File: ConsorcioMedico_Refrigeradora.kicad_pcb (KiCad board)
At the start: 2 copper layers, 260 x 70 mm, 111 parts, among them J1 BatteryHolder, J10 Screw_Terminal_01x01, J11 Screw_Terminal_01x01, J12 Screw_Terminal_01x01, J13 Screw_Terminal_01x01, J2 USART, J3 Screw_Terminal_01x01, J4 SWD, J5 Screw_Terminal_01x01, J6 Screw_Terminal_01x02, J7 Screw_Terminal_01x02, J8 Screw_Terminal_01x01, J9 Screw_Terminal_01x01, K1 HF46F-G/012-HS1T, K2 T9AS1D12-12, K4 HF46F-G/012-HS1T, Q1 MMBT3904, Q2 MMBT3904, Q3 MMBT3904, Q4 MMBT3904, Q5 BSS123, Q6 BSS123, Q7 BSS123, U1 STM32F411RETx, U2 IRM-02, U3 LDL1117, U4 INA350, U5 INA350, Y1 8Mhz, Y2 32.768khz/12.5pF

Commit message: SCH: Falta definir los capacitores de entrada, colocar el footprint del diodo e inductor. PCB: Falta acomodar algunos componentes.
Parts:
- removed D2, D3: RED, 1-Led:LED_0805
- removed J12, J13, J5: Screw_Terminal_01x01, 1-Pad:PAD_D2.60mm_Drill1.4mm
- added C27: 1uF 50V, 1-Capacitor:C_0805_2012Metric, B.Cu at (77.3, 94.9)
- added C28: 1uF 50V, 1-Capacitor:C_0805_2012Metric, B.Cu at (93.1, 96.4)
- added C29: 470uF, 1-Capacitor:C_1206_3216Metric, B.Cu at (47.5, 121.4)
- added C31: 1uF, 1-Capacitor:C_0805_2012Metric, B.Cu at (42.4, 127.7)
- added C32: 1uF, 1-Capacitor:C_0805_2012Metric, B.Cu at (42.4, 130.7)
- added C33: 180uF, 1-Capacitor:C_1206_3216Metric, B.Cu at (47.5, 128.1)
- added D10: 1N4148WS, Diode_SMD:D_SOD-323, B.Cu at (180.8, 85.9)
- added D11: RED, 1-Led:LED_0805, B.Cu at (71.8, 83.6)
- added D12: RED, 1-Led:LED_0805, B.Cu at (88.6, 83.7)
- added J16: Screw_Terminal_01x02, 1-Terminal-Block:DG504-5.08-02P_or_SMKDS 2,5-2-5.08, B.Cu at (72.6, 72.6)
- added J17: Screw_Terminal_01x02, 1-Terminal-Block:DG504-5.08-02P_or_SMKDS 2,5-2-5.08, B.Cu at (89.4, 72.5)
- added J19: Screw_Terminal_01x02, 1-Terminal-Block:DG504-5.08-02P_or_SMKDS 2,5-2-5.08, B.Cu at (165.0, 72.7)
- added JP1: Bridge1, Jumper:SolderJumper-2_P1.3mm_Open_Pad1.0x1.5mm, B.Cu at (85.3, 76.4)
- added JP2: Bridge1, Jumper:SolderJumper-2_P1.3mm_Open_Pad1.0x1.5mm, B.Cu at (68.5, 76.5)
- added K3: HF46F-G/012-HS1T, 1-Relay:Relay_HONGFA_SPST-NO_20.5x7x15.3mm, B.Cu at (155.1, 84.3)
- added Q8: BSS806, Package_TO_SOT_SMD:SOT-23, B.Cu at (183.8, 89.8)
- added R40: 10K, 1-Resistor:R_0805_2012Metric, B.Cu at (158.2, 89.6)
- added R41: 10K, 1-Resistor:R_0805_2012Metric, B.Cu at (180.8, 89.7)
- added R42: 6.2k, 1-Resistor:R_1206_3216Metric, B.Cu at (72.2, 79.3)
- added R43: 2.4k, 1-Resistor:R_0805_2012Metric, B.Cu at (71.6, 81.5)
- added R44: 1k, 1-Resistor:R_0805_2012Metric, B.Cu at (77.3, 92.8)
- added R45: 22k, 1-Resistor:R_0805_2012Metric, B.Cu at (77.3, 90.7)
- added R46: 6.2k, 1-Resistor:R_1206_3216Metric, B.Cu at (89.0, 79.4)
- added R47: 2.4k, 1-Resistor:R_0805_2012Metric, B.Cu at (88.4, 81.7)
- added R48: 1k, 1-Resistor:R_0805_2012Metric, B.Cu at (93.1, 94.4)
- added R49: 22k, 1-Resistor:R_0805_2012Metric, B.Cu at (93.1, 92.4)
- added R50: 2k, 1-Resistor:R_0805_2012Metric, B.Cu at (68.4, 72.8)
- added R51: 2k, 1-Resistor:R_0805_2012Metric, B.Cu at (85.3, 72.9)
- added U6: LTV-357T, Package_SO:SO-4_4.4x3.6mm_P2.54mm, B.Cu at (77.3, 85.1)
- added U7: LTV-357T, Package_SO:SO-4_4.4x3.6mm_P2.54mm, B.Cu at (93.0, 86.9)
- added U8: LM2594HVM-5.0, Package_SO:SOIC-8_3.9x4.9mm_P1.27mm, B.Cu at (40.4, 122.9)
- D1: value L-144IDT -> LED_0805; footprint 1-Led:LED_3.9x1.9mm -> 1-Led:LED_0805; moved to B.Cu
- D9: value LED_0805 -> L-144IDT; footprint 1-Led:LED_0805 -> 1-Led:LED_3.9x1.9mm
- J10, J11, J8, J9: value Screw_Terminal_01x01 -> Screw_Terminal_01x02; footprint 1-Pad:PAD_D2.60mm_Drill1.4mm -> 1-Terminal-Block:DG504-5.08-02P_or_SMKDS 2,5-2-5.08
- J3: value Screw_Terminal_01x01 -> USART; footprint 1-Pad:PAD_D2.60mm_Drill1.4mm -> 1-Pinhead:PinHeader_1x04_P2.54mm_Vertical
- Q5, Q6, Q7: value BSS123 -> BSS806
- R14: value 120R -> 1k
- R2, R4, R5: value 1k -> 330
- R24, R29: value 1k -> 2.2k
- R35, R36, R38: value 330 -> 1k
- R39: value 10K -> 220R
- R6: value 1k -> 120R
- moved R20 317.9 mm to (258.7, 101.7), turned to -90 degrees
- moved R19 293.3 mm to (233.9, 105.3), turned to 90 degrees
- moved D5 287.6 mm to (222.1, 90.0), turned to -90 degrees
- moved D4 267.4 mm to (201.8, 85.7)
- moved Q6 265.9 mm to (216.3, 89.5), turned to 0 degrees
- moved R15 264.7 mm to (209.5, 105.3), turned to 90 degrees
- moved Q5 254.6 mm to (204.7, 89.2), turned to 0 degrees
- moved R34 253.4 mm to (213.2, 89.5), turned to -90 degrees
- moved R32 246.5 mm to (211.1, 89.5), turned to -90 degrees
- moved R18 243.8 mm to (184.3, 105.2), turned to 90 degrees
- moved R33 242.0 mm to (201.6, 89.2), turned to -90 degrees
- moved R31 234.9 mm to (199.5, 89.2), turned to -90 degrees
- moved J4 230.2 mm to (145.2, 131.0), turned to -90 degrees
- moved D6 224.0 mm to (158.8, 85.9)
- moved R17 220.2 mm to (160.5, 105.5), turned to 90 degrees
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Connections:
- C13 pad 1: +5V -> +12V
- J2 pad 2: MCU_RX6 -> MCU_RX1
- J2 pad 3: MCU_TX6 -> MCU_TX1
- J3 pad 1: Net-(J3-Pin_1) -> +3.3V
- K1 pad 3: Net-(J9-Pin_1) -> Net-(J8-Pin_1)
- K1 pad 4: Net-(J8-Pin_1) -> Net-(J8-Pin_2)
- K2 pad 1: Net-(D6-A) -> Net-(D5-A)
- K2 pad 3: Net-(J13-Pin_1) -> Net-(J9-Pin_1)
- K2 pad 4: Net-(J12-Pin_1) -> Net-(J9-Pin_2)
- K4 pad 1: Net-(D5-A) -> Net-(D10-A)
- K4 pad 3: Net-(J11-Pin_1) -> Net-(J10-Pin_1)
- K4 pad 4: Net-(J10-Pin_1) -> Net-(J10-Pin_2)
- R1 pad 2: Net-(D9-A) -> Net-(D1-A)
- R11 pad 1: E -> C
- R11 pad 2: Net-(LED1-E) -> Net-(LED1-C)
- R12 pad 1: F -> B
- R12 pad 2: Net-(LED1-F) -> Net-(LED1-B)
- R13 pad 1: G -> A
- R13 pad 2: Net-(LED1-G) -> Net-(LED1-A)
- R14 pad 1: DP -> DIG1
- R14 pad 2: Net-(LED1-DP) -> Net-(Q1-B)
- R15 pad 1: Button_Touch -> Button_Buzzer
- R16 pad 1: Button_Up -> Button_Touch
- R17 pad 1: Button_Buzzer -> Button_Up
- R2 pad 1: DIG1 -> LED_Defrost
- R2 pad 2: Net-(Q1-B) -> Net-(D7-PadA)
- R21 pad 2: Net-(J7-Pin_1) -> Net-(J6-Pin_1)
- R22 pad 1: Net-(J7-Pin_1) -> Net-(J6-Pin_1)
- R23 pad 1: Net-(J7-Pin_2) -> Net-(J6-Pin_2)
- R24 pad 1: RTD1 -> I2C3_SCL
- R24 pad 2: Net-(D2-A) -> +3.3V
- R25 pad 1: Net-(J7-Pin_2) -> Net-(J6-Pin_2)
- R26 pad 2: Net-(J6-Pin_1) -> Net-(J7-Pin_1)
- R27 pad 1: Net-(J6-Pin_1) -> Net-(J7-Pin_1)
- R28 pad 1: Net-(J6-Pin_2) -> Net-(J7-Pin_2)
- R29 pad 1: RTD2 -> I2C3_SDA
- R29 pad 2: Net-(D3-A) -> +3.3V
- R30 pad 1: Net-(J6-Pin_2) -> Net-(J7-Pin_2)
- R31 pad 1: RELAY_Q1 -> Relay_Fan
- R32 pad 1: RELAY_Q3 -> Relay_Compressor
- R32 pad 2: Net-(Q7-G) -> Net-(Q6-G)
- R34 pad 2: Net-(Q7-G) -> Net-(Q6-G)
- R35 pad 1: LED_Defrost -> DIG2
- R35 pad 2: Net-(D1-PadA) -> Net-(Q2-B)
- R36 pad 1: LED_Door -> DIG3
- R36 pad 2: Net-(D7-PadA) -> Net-(Q3-B)
- R37 pad 1: RELAY_Q2 -> Relay_Light
- R37 pad 2: Net-(Q6-G) -> Net-(Q7-G)
- R38 pad 1: LED_TempAlarm -> DIG4
- R38 pad 2: Net-(D8-PadA) -> Net-(Q4-B)
- R39 pad 1: GND -> Relay_Calefac
- R39 pad 2: Net-(Q6-G) -> Net-(Q8-G)
- R4 pad 1: DIG2 -> LED_Door
- R4 pad 2: Net-(Q2-B) -> Net-(D8-PadA)
- R5 pad 1: DIG3 -> LED_TempAlarm
- R5 pad 2: Net-(Q3-B) -> Net-(D9-PadA)
- R6 pad 1: DIG4 -> DP
- R6 pad 2: Net-(Q4-B) -> Net-(LED1-DP)
- R7 pad 1: A -> G
- R7 pad 2: Net-(LED1-A) -> Net-(LED1-G)
- R8 pad 1: B -> F
- R8 pad 2: Net-(LED1-B) -> Net-(LED1-F)
- R9 pad 1: C -> E
- R9 pad 2: Net-(LED1-C) -> Net-(LED1-E)
- U1 pad 10: unconnected-(U1-PC2-Pad10) -> DIG2
- U1 pad 11: unconnected-(U1-PC3-Pad11) -> DIG1
- U1 pad 2: unconnected-(U1-PC13-Pad2) -> Relay_Calefac
- U1 pad 24: unconnected-(U1-PC4-Pad24) -> RTD1
- U1 pad 25: unconnected-(U1-PC5-Pad25) -> RTD2
- U1 pad 33: STATUS_LED -> LED_Status
- U1 pad 34: unconnected-(U1-PB13-Pad34) -> LED_Defrost
- U1 pad 35: unconnected-(U1-PB14-Pad35) -> LED_Door
- U1 pad 36: unconnected-(U1-PB15-Pad36) -> LED_TempAlarm
- U1 pad 38: unconnected-(U1-PC7-Pad38) -> DIG_IN_1
- U1 pad 39: unconnected-(U1-PC8-Pad39) -> DIG_IN_0
- U1 pad 40: unconnected-(U1-PC9-Pad40) -> I2C3_SDA
- U1 pad 41: DIG1 -> I2C3_SCL
- U1 pad 42: DIG2 -> MCU_TX1
- U1 pad 43: DIG3 -> MCU_RX1
- U1 pad 44: DIG4 -> USB_DM
- U1 pad 45: LED_Status -> USB_DP
- U1 pad 46: LED_Defrost -> SWDIO
- U1 pad 49: LED_Door -> SWCLK
- U1 pad 50: LED_TempAlarm -> unconnected-(U1-PA15-Pad50)
- U1 pad 51: unconnected-(U1-PC10-Pad51) -> Relay_Fan
- U1 pad 52: unconnected-(U1-PC11-Pad52) -> Relay_Light
- U1 pad 53: unconnected-(U1-PC12-Pad53) -> Relay_Compressor
- U1 pad 55: Button_Buzzer -> SWO
- U1 pad 56: Button_Touch -> Button_Buzzer
- U1 pad 57: Button_Up -> Button_Touch
- U1 pad 58: Button_Down -> Button_Up
- U1 pad 59: Button_Cooling -> Button_Down
- U1 pad 61: Button_Light -> Button_Cooling
- U1 pad 62: unconnected-(U1-PB9-Pad62) -> Button_Light
- U1 pad 8: unconnected-(U1-PC0-Pad8) -> DIG4
- U1 pad 9: unconnected-(U1-PC1-Pad9) -> DIG3
- U2 pad +V: +5V -> +12V
- U2 pad AC1: Net-(J3-Pin_1) -> Net-(J11-Pin_1)
- U2 pad AC2: Net-(J5-Pin_1) -> Net-(J11-Pin_2)

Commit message: SCH: Se cambió el IRM, se colocó filtro en la entrada AC, se modificó la fuente switching LM, se corrigieron algunos errores de diseño. PCB: Se terminó el placement de los componentes
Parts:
- removed C31, C32: 1uF, 1-Capacitor:C_0805_2012Metric
- removed C33: 180uF, 1-Capacitor:C_1206_3216Metric
- removed U2: IRM-02, 1-Supply_Module-Eagle:IRM-02
- added C30: 0.1uF 275VAC, Capacitor_THT:C_Rect_L18.0mm_W5.0mm_P15.00mm_FKS3_FKP3, B.Cu at (122.0, 65.9)
- added C35: 220uF 25V, Capacitor_SMD:CP_Elec_6.3x7.7, B.Cu at (101.0, 103.0)
- added D2: SS34B, 1-Diode:D_SMB, B.Cu at (101.0, 93.3)
- added F1: Fuse, Fuse:Fuseholder_TR5_Littelfuse_No560_No460, B.Cu at (138.1, 69.1)
- added L1: YSPI1050-680M, Inductor_SMD:L_10.4x10.4_H4.8, B.Cu at (110.2, 95.3)
- added L2: UU9.8-10mH, 1-Inductor:UU9.8-10mH, B.Cu at (119.1, 80.7)
- added R52: 1k, 1-Resistor:R_0603_1608Metric, B.Cu at (94.4, 88.0)
- added RV1: FNR6045S680, Varistor:RV_Disc_D12mm_W5.1mm_P7.5mm, B.Cu at (126.5, 66.7)
- added U9: HLK-PMx, 1-Module:HLK-PM12, B.Cu at (106.9, 84.2)
- C13: value 10uF -> 470uF 25V; footprint 1-Capacitor:C_1206_3216Metric -> Capacitor_SMD:CP_Elec_10x10
- C29: value 470uF -> 220uF 25V; footprint 1-Capacitor:C_1206_3216Metric -> Capacitor_SMD:CP_Elec_6.3x7.7
- K2: value T9AS1D12-12 -> AZ2150-1A-12DEF; footprint 1-Relay:Relay_TE-Connectivity_SPST-NO_32.5x27.4x27.9mm -> 1-Relay:Relay_Zettler_SPST-NO_31.8x26.9x19.1mm
- moved J11 120.9 mm to (143.4, 72.7)
- moved C12 102.9 mm to (29.8, 116.4), turned to 180 degrees
- moved J1 102.2 mm to (26.7, 116.3)
- moved J3 85.5 mm to (81.8, 131.5)
- moved C13 65.6 mm to (87.4, 92.6), turned to -90 degrees
- moved R2 62.9 mm to (15.9, 96.5), turned to 180 degrees
- moved U8 62.7 mm to (95.7, 93.4), turned to 90 degrees
- moved R4 59.8 mm to (15.9, 105.5), turned to 180 degrees
- moved R5 56.4 mm to (15.8, 114.4), turned to 180 degrees
- moved C28 54.2 mm to (39.5, 89.0), turned to -90 degrees
- moved R48 51.9 mm to (41.5, 89.0), turned to 90 degrees
- moved R47 51.6 mm to (36.8, 81.8)
- moved J17 51.6 mm to (37.8, 72.7)
- moved R46 51.6 mm to (37.4, 79.5)
- moved D12 51.6 mm to (37.0, 83.8)
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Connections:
- C29 pad 1: GND -> +12V
- C29 pad 2: +12V -> GND
- D10 pad 1: +5V -> +12V
- D4 pad 1: +5V -> +12V
- D5 pad 1: +5V -> +12V
- D6 pad 1: +5V -> +12V
- K1 pad 2: +5V -> +12V
- K2 pad 2: +5V -> +12V
- K3 pad 2: +5V -> +12V
- K4 pad 2: +5V -> +12V
- U8 pad 5: unconnected-(U8-~{ON}/OFF-Pad5) -> Net-(U8-~{ON}/OFF)

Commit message: Se guarda avance
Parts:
- moved J1 2.11 mm to (26.9, 118.4)
- moved C12 2.11 mm to (30.0, 118.5)
- moved C6 2.09 mm to (69.3, 125.1)
- moved C7 2.09 mm to (70.9, 125.1)
- moved U1 1.34 mm to (66.6, 116.8)
- moved C20 1.34 mm to (63.9, 125.2)
- moved C4 1.34 mm to (58.3, 111.0)
- moved C11 1.34 mm to (71.7, 107.8)
- moved C15 1.34 mm to (75.2, 123.7)
- moved C17 1.34 mm to (80.2, 113.2)
- moved C18 1.34 mm to (80.2, 110.2)
- moved D1 1.34 mm to (55.6, 123.7)
- moved R1 1.34 mm to (55.5, 121.7)
- moved C10 1.34 mm to (73.5, 107.8)
- moved C5 1.34 mm to (58.3, 112.6)
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
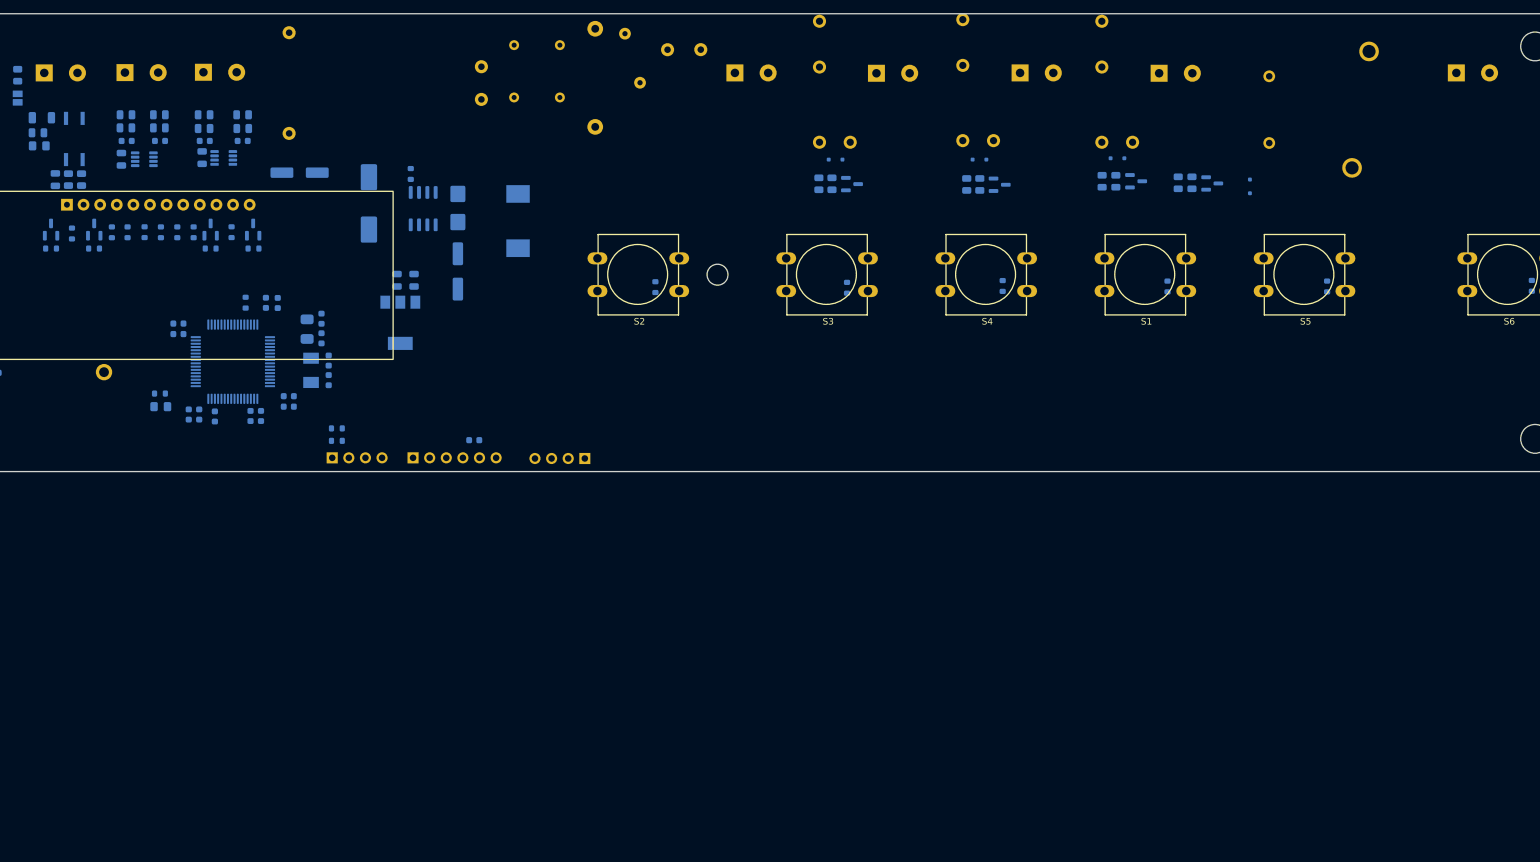
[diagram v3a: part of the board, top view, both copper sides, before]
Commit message: SCH: Se cambian la bornera por terminales, se añade un disparo más para el compressor (falta conectarlo al uC), falta modificar, se cambia la fuente switching por otra de menos costo
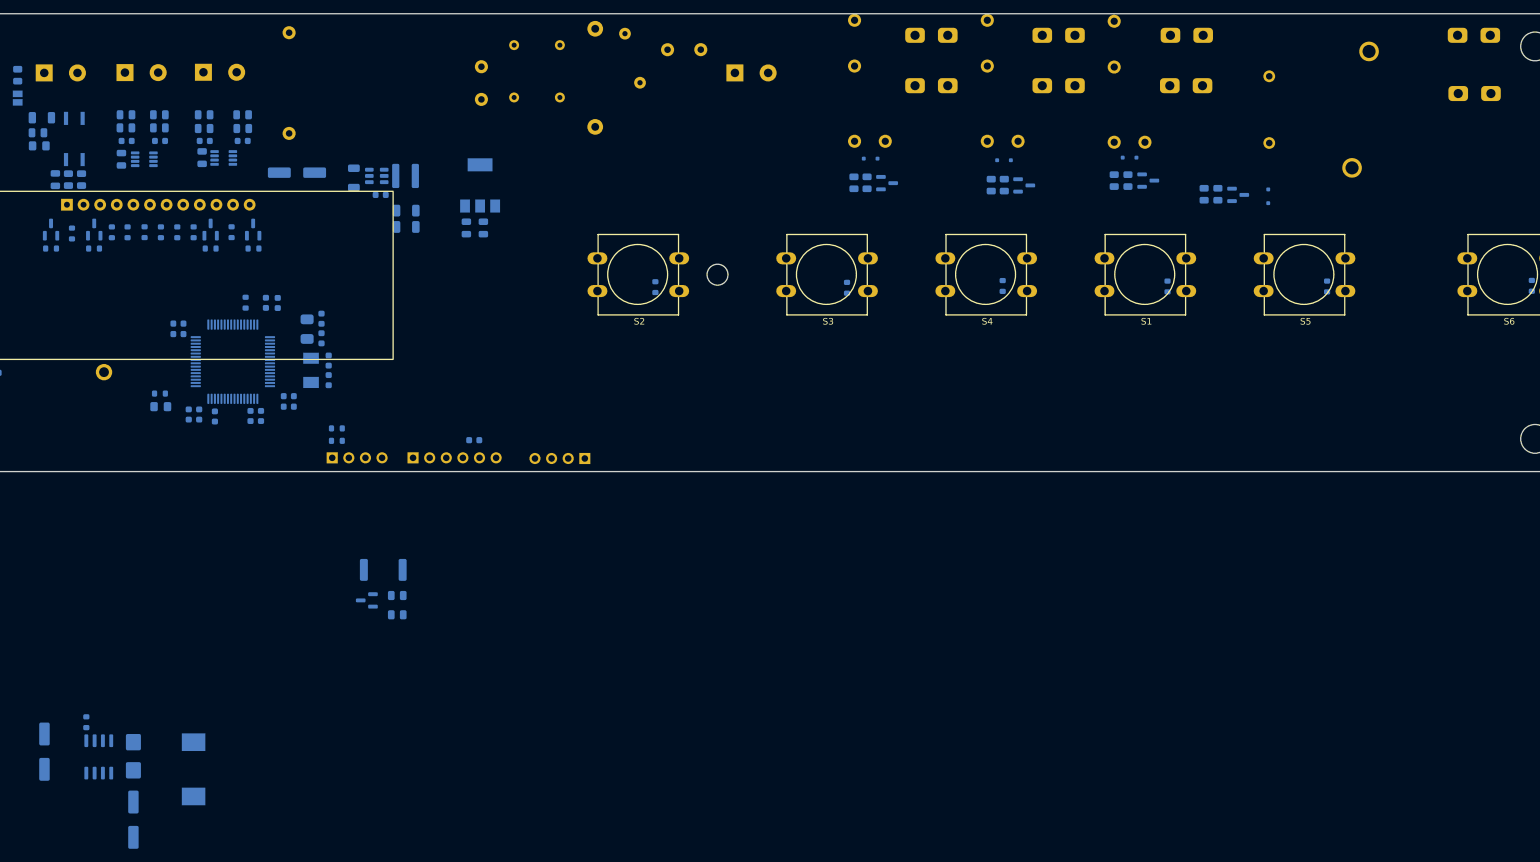
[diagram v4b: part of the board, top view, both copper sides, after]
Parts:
- removed J10, J19: Screw_Terminal_01x02, 1-Terminal-Block:DG504-5.08-02P_or_SMKDS 2,5-2-5.08
- added C31: 10uF, 1-Capacitor:C_1206_3216Metric, B.Cu at (85.1, 88.7)
- added C32: 22uF, 1-Capacitor:C_1206_3216Metric, B.Cu at (93.1, 93.7)
- added C33: 22uF, 1-Capacitor:C_1206_3216Metric, B.Cu at (93.1, 96.2)
- added C36: 100nF, 1-Capacitor:C_0603_1608Metric, B.Cu at (89.2, 91.3)
- added J12: Light, 1-Pad:Solder-Terminal_FS1536_6.3x0.8mm_NINIGI, B.Cu at (177.4, 67.3)
- added J13: Light, 1-Pad:Solder-Terminal_FS1536_6.3x0.8mm_NINIGI, B.Cu at (177.4, 75.0)
- added J14: Compress, 1-Pad:Solder-Terminal_FS1536_6.3x0.8mm_NINIGI, B.Cu at (252.4, 75.4)
- added J15: Resistor, 1-Pad:Solder-Terminal_FS1536_6.3x0.8mm_NINIGI, B.Cu at (196.8, 67.3)
- added J18: Resistor, 1-Pad:Solder-Terminal_FS1536_6.3x0.8mm_NINIGI, B.Cu at (196.8, 75.0)
- added J5: Evap_fan, 1-Pad:Solder-Terminal_FS1536_6.3x0.8mm_NINIGI, B.Cu at (208.4, 66.5)
- added L3: YNR4030-4R7M 4.7uF, 1-Inductor:Inductor_YNR4030_4x4x3mm_YJYCOIN, B.Cu at (91.0, 90.4)
- added Q9: BSS806, Package_TO_SOT_SMD:SOT-23, B.Cu at (87.1, 153.3)
- added R53: 150R, 1-Resistor:R_2512_6332Metric, B.Cu at (89.6, 148.6)
- added R54: 220R, 1-Resistor:R_0805_2012Metric, B.Cu at (91.7, 152.6)
- added R55: 10K, 1-Resistor:R_0805_2012Metric, B.Cu at (91.7, 155.5)
- added U2: AP63205WU, Package_TO_SOT_SMD:TSOT-23-6, B.Cu at (88.6, 88.4)
- C13: value 470uF 25V -> 68uF 25V; footprint Capacitor_SMD:CP_Elec_10x10 -> Capacitor_SMD:CP_Elec_6.3x5.7
- C29: value 220uF 25V -> 100uF 25V
- J8: value Screw_Terminal_01x02 -> Evap_fan; footprint 1-Terminal-Block:DG504-5.08-02P_or_SMKDS 2,5-2-5.08 -> 1-Pad:Solder-Terminal_FS1536_6.3x0.8mm_NINIGI
- J9: value Screw_Terminal_01x02 -> Compress; footprint 1-Terminal-Block:DG504-5.08-02P_or_SMKDS 2,5-2-5.08 -> 1-Pad:Solder-Terminal_FS1536_6.3x0.8mm_NINIGI
- moved C13 97.4 mm to (37.8, 176.4)
- moved R52 97.4 mm to (44.2, 171.9)
- moved D2 97.4 mm to (51.4, 177.1)
- moved L1 97.4 mm to (60.6, 179.1)
- moved C35 97.4 mm to (51.4, 186.8)
- moved U8 97.4 mm to (46.1, 177.2)
- moved U3 24.3 mm to (104.4, 89.8), turned to 90 degrees
- moved C19 15.4 mm to (104.9, 96.3), turned to -90 degrees
- moved C14 11.3 mm to (102.3, 96.3), turned to -90 degrees
- moved J9 8.57 mm to (260.4, 67.3), turned to 180 degrees
- moved D6 5.36 mm to (164.1, 85.8)
- moved K3 5.36 mm to (160.5, 84.2)
- moved Q7 5.36 mm to (166.6, 89.5)
- moved R37 5.36 mm to (161.6, 89.5)
- moved R40 5.36 mm to (163.6, 89.5)
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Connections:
- K1 pad 4: Net-(J8-Pin_2) -> Net-(J5-Pin_1)
- K2 pad 3: Net-(J9-Pin_1) -> Net-(J14-Pin_1)
- K2 pad 4: Net-(J9-Pin_2) -> Net-(J9-Pin_1)

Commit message: SCH: Se modificó la posición de algunos pines para mejorar la calidad del ruteado. PCB: Se enruta las señales, quedando la alimentación, pines de programación, relays y planos de gnd
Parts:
- removed C13: 68uF 25V, Capacitor_SMD:CP_Elec_6.3x5.7
- removed C35: 220uF 25V, Capacitor_SMD:CP_Elec_6.3x7.7
- removed D2: SS34B, 1-Diode:D_SMB
- removed J17, J6, J7: Screw_Terminal_01x02, 1-Terminal-Block:DG504-5.08-02P_or_SMKDS 2,5-2-5.08
- removed L1: YSPI1050-680M, Inductor_SMD:L_10.4x10.4_H4.8
- removed R52: 1k, 1-Resistor:R_0603_1608Metric
- removed U8: LM2594HVM-5.0, Package_SO:SOIC-8_3.9x4.9mm_P1.27mm
- added J10: AC, 1-Pad:Solder-Terminal_FS1536_6.3x0.8mm_NINIGI, B.Cu at (141.8, 74.2)
- added J19: AC, 1-Pad:Solder-Terminal_FS1536_6.3x0.8mm_NINIGI, B.Cu at (141.8, 66.5)
- F1: value Fuse -> 250VAC 0.5AAC
- J11: value Screw_Terminal_01x02 -> Digital; footprint 1-Terminal-Block:DG504-5.08-02P_or_SMKDS 2,5-2-5.08 -> 1-Terminal-Block:Terminal-Block_XY2500V-B_4P_P5.0mm_XINYA
- J16: value Screw_Terminal_01x02 -> Analog; footprint 1-Terminal-Block:DG504-5.08-02P_or_SMKDS 2,5-2-5.08 -> 1-Terminal-Block:Terminal-Block_XY2500V-B_4P_P5.0mm_XINYA
- moved R53 145.3 mm to (222.9, 90.9)
- moved Q9 140.7 mm to (214.3, 93.3), turned to 0 degrees
- moved R55 134.8 mm to (211.3, 93.3), turned to -90 degrees
- moved R54 131.7 mm to (209.3, 93.3), turned to -90 degrees
- moved J11 111.3 mm to (32.2, 68.0)
- moved C1 54.4 mm to (50.4, 116.9), turned to 90 degrees
- moved J4 52.3 mm to (47.7, 107.5), turned to 180 degrees
- moved J16 35.6 mm to (59.8, 68.0)
- moved J3 30.9 mm to (111.9, 124.6), turned to 90 degrees
- moved C18 30.0 mm to (54.4, 125.6), turned to 180 degrees
- moved R29 29.6 mm to (111.4, 122.4), turned to 0 degrees
- moved R24 29.0 mm to (111.5, 126.9), turned to 0 degrees
- moved C2 27.7 mm to (53.7, 120.0), turned to 90 degrees
- moved C3 27.7 mm to (53.7, 116.8), turned to -90 degrees
- moved C17 27.4 mm to (54.4, 122.7), turned to 180 degrees
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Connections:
- C30 pad 2: Net-(J11-Pin_2) -> Net-(J10-Pin_1)
- C32 pad 1: Net-(U2-FB) -> +5V
- C33 pad 1: Net-(U2-FB) -> +5V
- F1 pad 1: Net-(J11-Pin_1) -> Net-(J19-Pin_1)
- J11 pad 1: Net-(J11-Pin_1) -> I0
- J11 pad 2: Net-(J11-Pin_2) -> GND
- J16 pad 1: I0 -> Net-(J16-Pin_1)
- J16 pad 2: GND -> Net-(J16-Pin_2)
- L2 pad 1: Net-(J11-Pin_2) -> Net-(J10-Pin_1)
- L3 pad 2: Net-(U2-FB) -> +5V
- R21 pad 2: Net-(J6-Pin_1) -> Net-(J16-Pin_1)
- R22 pad 1: Net-(J6-Pin_1) -> Net-(J16-Pin_1)
- R23 pad 1: Net-(J6-Pin_2) -> Net-(J16-Pin_2)
- R25 pad 1: Net-(J6-Pin_2) -> Net-(J16-Pin_2)
- R26 pad 2: Net-(J7-Pin_1) -> Net-(J16-Pin_3)
- R27 pad 1: Net-(J7-Pin_1) -> Net-(J16-Pin_3)
- R28 pad 1: Net-(J7-Pin_2) -> Net-(J16-Pin_4)
- R30 pad 1: Net-(J7-Pin_2) -> Net-(J16-Pin_4)
- RV1 pad 2: Net-(J11-Pin_2) -> Net-(J10-Pin_1)
- U1 pad 2: Relay_Calefac -> unconnected-(U1-PC13-Pad2)
- U1 pad 33: LED_Status -> Relay_Light
- U1 pad 34: LED_Defrost -> Relay_Calefac
- U1 pad 35: LED_Door -> Relay_Fan
- U1 pad 36: LED_TempAlarm -> Relay_Compressor
- U1 pad 37: unconnected-(U1-PC6-Pad37) -> Relay_Compressor_Save
- U1 pad 38: DIG_IN_1 -> Button_Touch
- U1 pad 39: DIG_IN_0 -> Button_Up
- U1 pad 51: Relay_Fan -> Button_Down
- U1 pad 52: Relay_Light -> Button_Buzzer
- U1 pad 53: Relay_Compressor -> Button_Cooling
- U1 pad 54: unconnected-(U1-PD2-Pad54) -> Button_Light
- U1 pad 56: Button_Buzzer -> DIG_IN_0
- U1 pad 57: Button_Touch -> DIG_IN_1
- U1 pad 58: Button_Up -> LED_Status
- U1 pad 59: Button_Down -> LED_TempAlarm
- U1 pad 61: Button_Cooling -> LED_Door
- U1 pad 62: Button_Light -> LED_Defrost
- U2 pad 1: Net-(U2-FB) -> +5V
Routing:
- net Button_Light: track 0.00 -> 215.7 mm
- net +12V: track 0.00 -> 179.9 mm, vias 0 -> 5
- net Button_Cooling: track 0.00 -> 178.5 mm
- net +3.3V: track 0.00 -> 169.9 mm, vias 0 -> 7
- net Button_Buzzer: track 0.00 -> 158.3 mm
- net Relay_Compressor: track 0.00 -> 155.7 mm
- net Relay_Compressor_Save: track 0.00 -> 154.3 mm
- net Relay_Fan: track 0.00 -> 143.6 mm
- net Button_Down: track 0.00 -> 135.2 mm
- net Relay_Calefac: track 0.00 -> 122.7 mm
- net Relay_Light: track 0.00 -> 101.4 mm
- net Button_Up: track 0.00 -> 100.7 mm
- net DIG_IN_0: track 0.00 -> 78.5 mm, vias 0 -> 2
- net DIG_IN_1: track 0.00 -> 74.5 mm, vias 0 -> 2
- net LED_Defrost: track 0.00 -> 70.7 mm
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- added copper zone on B.Cu, net +12V
- added copper zone on B.Cu, net +5V
- added copper zone on B.Cu, net Net-(U2-SW)
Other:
- board text removed: "77.5"
